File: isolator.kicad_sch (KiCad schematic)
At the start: 120 parts, among them J1 HOST, J2 USB_C_Receptacle_PowerOnly_6P, J3 USB_A, J4 USB_A, J5 USB_C_Receptacle_USB2.0_16P, J6 USB_C_Receptacle_USB2.0_16P, Q1 2N7002, Q2 2N7002, T1 750313638, U1 ADuM4165, U10 TPS2553DBV, U11 TPS2553DBV, U12 TPS2553DBV, U13 TLV7041DBV, U14 TLV7041DBV, U15 NUP4202, U16 NUP4202, U17 NUP4202, U18 NUP4202, U2 NUP4202, U3 NUP4202, U4 USB2514B_Bi, U5 SN6505BDBV, U6 MIC29302WU, U7 TPS2121, U8 AP2112K-3.3, U9 TPS2553DBV, Y1 24M 8pF, Y2 24M 12pF

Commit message: chore(sch): carry GUI session edits; restore U7 OV2 ground wires lost in GUI edit
Co-Authored-By: Claude Fable 5 <noreply@anthropic.com>
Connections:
- net HOST_D+: now also U2.1; no longer U2.6
- net HOST_D-: now also U2.6; no longer U2.1

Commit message: feat: swap NUP4202 ESD for flow-through USBLC6-2SC6 (sch+pcb), symmetric USB pair routing
Replaces all six NUP4202 SOT-363 ESD arrays (U2 host, U3 hub-upstream,
U15-U18 downstream ports) with USBLC6-2SC6 in SOT-23-6.

The NUP4202 pinout forced each USB HS pair to split - one line off the top
of the package, the other off the bottom - so the pairs could not be routed
symmetrically. The USBLC6-2SC6 is flow-through: I/O1 appears on pins 1 and 6,
I/O2 on pins 3 and 4, so a pair enters one edge and leaves the opposite edge
at constant 1.9 mm spacing with no crossing.

Schematic:
- lib_symbols cache: NUP4202 removed, USBLC6-2SC6 added (flattened from the
  stock Power_Protection library, which defines it as extends USBLC6-2P6).
- All six sites redrawn flow-through at rot 0: D+ on pins 1/6 (left/right),
  D- on pins 3/4, VBUS up, GND down. Stale pin-3/4 no_connects removed.
- Properties: Value/Footprint/Datasheet updated; MPN USBLC6-2SC6,
  Manufacturer STMicroelectronics, LCSC C2687116 (SOT-23-6 variant - the
  commonly quoted C7519 is the SOT-23-6L package and does not match).
- Symbol UUIDs preserved so the schematic<->PCB links survive.

PCB:
- SOT-363 footprints replaced with SOT-23-6, entry row (pads 1/2/3) facing
  the connector/source side at each site.
- U17 and U18 nudged (the SOT-23-6 is 1.6 mm wider than the SOT-363 and
  collided with J5/J6): U17 160.5,95.0 -> 159.3,95.0; U18 160.5,110.0 ->
  159.4,106.7 with its refdes moved above the body to clear C43.

Gates: schematic ERC exit 0 (0 errors, no new warnings); PCB reloads;
DRC no new violation types, creepage still exactly 1 (the known C49 finding),
silk_overlap 11->10; unconnected 333->345 (+12, expected: pads 3/4 now carry
real nets instead of unconnected-(Ux-PadN)); 36/36 pads verified identical
between the schematic netlist export and the board.

Spec updated, including the eval-board rationale sentence: the core still
matches EVAL-ADuM4165 except for this deliberate ESD deviation.

Co-Authored-By: Claude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
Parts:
- U15, U16, U17, U18, U2, U3: value NUP4202 -> USBLC6-2SC6; footprint Package_TO_SOT_SMD:SOT-363_SC-70-6 -> Package_TO_SOT_SMD:SOT-23-6; symbol Power_Protection:NUP4202 -> Power_Protection:USBLC6-2SC6; LCSC C2937014 -> C2687116; MPN NUP4202W1T2G -> USBLC6-2SC6; Manufacturer onsemi -> STMicroelectronics
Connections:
- net HOST_D+: now also U2.6 (I/O1)
- net HOST_D-: now also U2.3 (I/O2), U2.4 (I/O2); no longer U2.6
- net ISO_D+: now also U3.1 (I/O1)
- net ISO_D-: now also U3.3 (I/O2), U3.4 (I/O2); no longer U3.1
- net P1_D+: now also U15.1 (I/O1)
- net P1_D-: now also U15.3 (I/O2), U15.4 (I/O2); no longer U15.1
- net P2_D+: now also U16.1 (I/O1)
- net P2_D-: now also U16.3 (I/O2), U16.4 (I/O2); no longer U16.1
- net P3_D+: now also U17.1 (I/O1)
- net P3_D-: now also U17.3 (I/O2), U17.4 (I/O2); no longer U17.1
- net P4_D+: now also U18.1 (I/O1)
- net P4_D-: now also U18.3 (I/O2), U18.4 (I/O2); no longer U18.1
- no-connect marks 19 -> 7

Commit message: feat(pcb): extend barrier slot under C49 (now 2220), rounded corners with concentric mounting holes, corrected 90R diff geometry per JLC-7628
Co-Authored-By: Claude Fable 5 <noreply@anthropic.com>
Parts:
- C49: footprint Capacitor_SMD:C_1812_4532Metric -> Capacitor_SMD:C_2220_5750Metric
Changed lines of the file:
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@@
 			)
 		)
-		(property "Footprint" "Capacitor_SMD:C_1812_4532Metric"
+		(property "Footprint" "Capacitor_SMD:C_2220_5750Metric"
 			(at 185.42 40.64 0)
 			(hide yes)

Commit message: wip(pcb): routing session 2 — GND stitching pours, more escapes
Co-Authored-By: Claude Fable 5 <noreply@anthropic.com>
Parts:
- added C50: 100n, Capacitor_SMD:C_0603_1608Metric, symbol Device:C_Small
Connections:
- net GND1: now also C50.2
- net GND2: no longer U7.4 (OV2)
- net VBUS_HOST: now also C50.1
- net at T1.1 (N1): now also U5.3 (D2); no longer U5.1 (D1)
- net at T1.3 (N2): now also U5.1 (D1); no longer U5.3 (D2)

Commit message: fix: decoupling audit fixes — tantalum C10 (T491D, polarity-correct), R36 330R min-load, 22u port bulk, re-seat ISO_5V bypass caps at their ICs per datasheet distances
Co-Authored-By: Claude Fable 5 <noreply@anthropic.com>
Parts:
- C10: footprint Capacitor_SMD:C_1210_3225Metric -> Capacitor_Tantalum_SMD:CP_EIA-7343-31_Kemet-D; MPN TMK325ABJ476MM-P -> T491D476K010AT
- C38, C41, C44, C47: value 10u -> 22u; MPN CL21A106KAYNNNE -> GRM21BR61A226ME44L
- R36: value 1k -> 330R; MPN RC0603FR-071KL -> RC0603FR-07330RL
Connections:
- net DCDC_5V: now also C10.1; no longer C10.2
- net GND2: now also C10.2, U7.4 (OV2); no longer C10.1
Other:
- moved on the sheet: C10
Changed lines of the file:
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@@
 			)
 		)
-		(property "Value" "10u"
+		(property "Value" "22u"
 			(at 171.45 345.4462 0)
 			(show_name no)
@@
 			)
 		)
-		(property "MPN" "CL21A106KAYNNNE"
+		(property "MPN" "GRM21BR61A226ME44L"
 			(at 168.91 344.17 0)
 			(hide yes)
@@
 			)
 		)
-		(property "Value" "10u"
+		(property "Value" "22u"
 			(at 133.35 400.0562 0)
 			(show_name no)
@@
 			)
 		)
-		(property "MPN" "CL21A106KAYNNNE"
+		(property "MPN" "GRM21BR61A226ME44L"
 			(at 130.81 398.78 0)
 			(hide yes)
@@
 			)
 		)
-		(property "Value" "10u"
+		(property "Value" "22u"
 			(at 294.64 345.4462 0)
 			(show_name no)
@@
 			)
 		)
-		(property "MPN" "CL21A106KAYNNNE"
+		(property "MPN" "GRM21BR61A226ME44L"
 			(at 292.1 344.17 0)
 			(hide yes)
@@
 			)
 		)
-		(property "Value" "10u"
+		(property "Value" "22u"
 			(at 83.82 345.4462 0)
 			(show_name no)
@@
 			)
 		)
-		(property "MPN" "CL21A106KAYNNNE"
+		(property "MPN" "GRM21BR61A226ME44L"
 			(at 81.28 344.17 0)
 			(hide yes)
@@
 	(symbol
 		(lib_id "Device:C_Small")
-		(at 619.76 44.45 180)
+		(at 619.76 44.45 0)
 		(unit 1)
 		(body_style 1)
@@
 			)
 		)
-		(property "Footprint" "Capacitor_SMD:C_1210_3225Metric"
+		(property "Footprint" "Capacitor_Tantalum_SMD:CP_EIA-7343-31_Kemet-D"
 			(at 619.76 44.45 0)
 			(hide yes)
@@
 			)
 		)
-		(property "MPN" "TMK325ABJ476MM-P"
+		(property "MPN" "T491D476K010AT"
 			(at 619.76 44.45 0)
 			(hide yes)
@@
 			)
 		)
-		(property "Value" "1k"
+		(property "Value" "330R"
 			(at 504.19 303.5299 0)
 			(show_name no)
@@
 			)
 		)
-		(property "MPN" "RC0603FR-071KL"
+		(property "MPN" "RC0603FR-07330RL"
 			(at 501.65 302.26 0)
 			(hide yes)
@@
 		)
 	)
+	(wire
+		(pts
+			(xy 193.04 176.53) (xy 199.39 176.53)
+		)
+		(stroke
+			(width 0)
+			(type default)
+		)
+	)
+	(wire
+		(pts
+			(xy 195.58 181.61) (xy 195.58 176.53)
+		)
+		(stroke
+			(width 0)
+			(type default)
+		)
+	)
+	(wire
+		(pts
+			(xy 195.58 176.53) (xy 201.93 176.53)
+		)
+		(stroke
+			(width 0)
+			(type default)
+		)
+	)

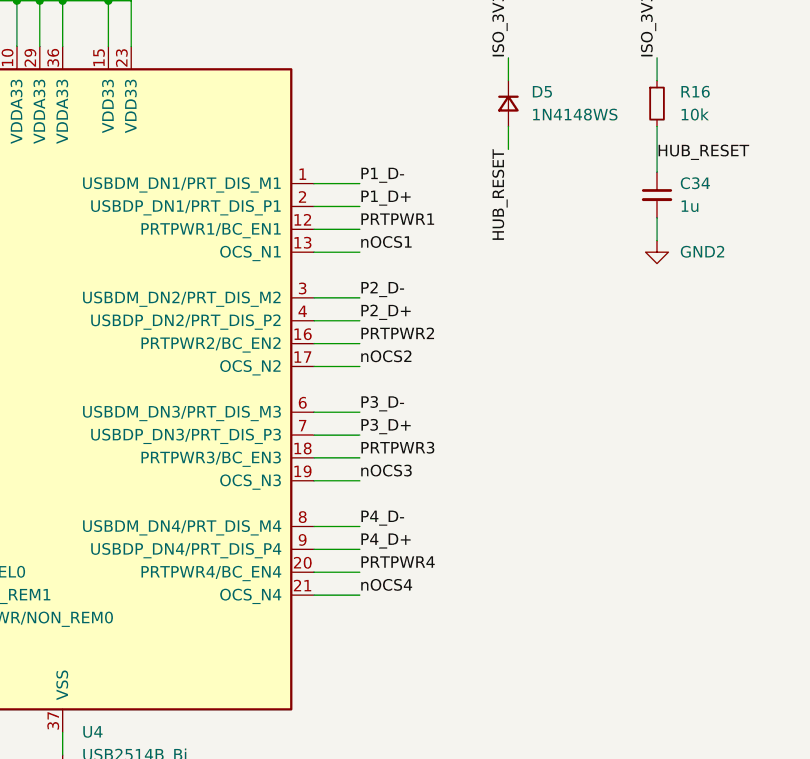
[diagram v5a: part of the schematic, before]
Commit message: feat: swap hub port bundles 1<->4 2<->3 for crossing-free fanout (sch+pcb)
U4 (USB2514B) is at rot 0 with all four downstream port pin bundles on its
WEST edge, while all four ports are on the far EAST side and are approached
heading east.  Any path from "heading west" to "heading east" is a 180 degree
turn, which reverses the transverse order of the ribbon: the pairs left U4 as
P1,P2,P3,P4 (north->south) and arrived as P4,P3,P2,P1, while the destinations
need P1,P2,P3,P4.  That is a full reversal of four items = 6 pair-to-pair
crossings, i.e. at least three crossunders (12 vias) on 480 Mbit/s pairs.
No rotation of U4 fixes it - handedness is preserved under rotation.

Hub ports 1-4 are functionally identical, so the fix is a net swap, not copper.
Full bundles move together (data pair + PRTPWR/BC_EN + OCS_N) so each port's
power switch and fault line stay with their own data pair:

  hub port1 <- port4   hub port2 <- port3
  hub port3 <- port2   hub port4 <- port1

Schematic: the 16 net labels on U4's downstream pin column (x = 463.55) were
renamed.  Nothing else moved - connector-side nets, TPS2553 switches, ILIM
resistors, ESD parts and VBUS are untouched.

PCB: the 16 affected U4 pads were re-netted in a mutation-only session, each
one cross-checked against a fresh `kicad-cli sch export netlist` before saving;
all 37 U4 pads verified to match the netlist afterwards.

Verification
  ERC severity-error: 0 violations, exit 0
  /PnD+- now = {U4 <new pin>, USBLC6 x2, connector}
    P1 -> U4 pins 8/9 (was 1/2)   P2 -> pins 6/7   P3 -> pins 3/4   P4 -> 1/2
  /PRTPWRn = exactly {U4 pin, TPS2553 pin 3} for all four
  /nOCSn   = {U4 pin, TPS2553 pin 4, pull-up} for all four
  GND1 n GND2 = {U1, C49} unchanged
  DRC unchanged: 102 violations, 170 unconnected, shorting 0, dangling 0

Co-Authored-By: Claude Fable 5 <noreply@anthropic.com>
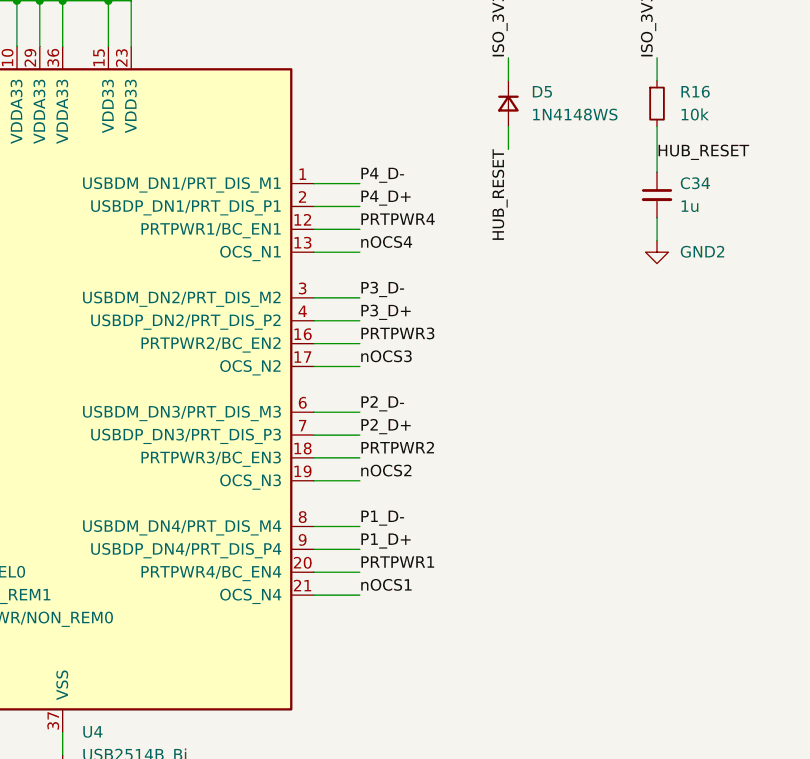
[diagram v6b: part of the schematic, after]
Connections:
- net P1_D+: now also U4.9 (USBDP_DN4/PRT_DIS_P4); no longer U4.2 (USBDP_DN1/PRT_DIS_P1)
- net P1_D-: now also U4.8 (USBDM_DN4/PRT_DIS_M4); no longer U4.1 (USBDM_DN1/PRT_DIS_M1)
- net P2_D+: now also U4.7 (USBDP_DN3/PRT_DIS_P3); no longer U4.4 (USBDP_DN2/PRT_DIS_P2)
- net P2_D-: now also U4.6 (USBDM_DN3/PRT_DIS_M3); no longer U4.3 (USBDM_DN2/PRT_DIS_M2)
- net P3_D+: now also U4.4 (USBDP_DN2/PRT_DIS_P2); no longer U4.7 (USBDP_DN3/PRT_DIS_P3)
- net P3_D-: now also U4.3 (USBDM_DN2/PRT_DIS_M2); no longer U4.6 (USBDM_DN3/PRT_DIS_M3)
- net P4_D+: now also U4.2 (USBDP_DN1/PRT_DIS_P1); no longer U4.9 (USBDP_DN4/PRT_DIS_P4)
- net P4_D-: now also U4.1 (USBDM_DN1/PRT_DIS_M1); no longer U4.8 (USBDM_DN4/PRT_DIS_M4)
- net PRTPWR1: now also U4.20 (PRTPWR4/BC_EN4); no longer U4.12 (PRTPWR1/BC_EN1)
- net PRTPWR2: now also U4.18 (PRTPWR3/BC_EN3); no longer U4.16 (PRTPWR2/BC_EN2)
- net PRTPWR3: now also U4.16 (PRTPWR2/BC_EN2); no longer U4.18 (PRTPWR3/BC_EN3)
- net PRTPWR4: now also U4.12 (PRTPWR1/BC_EN1); no longer U4.20 (PRTPWR4/BC_EN4)
- net nOCS1: now also U4.21 (OCS_N4); no longer U4.13 (OCS_N1)
- net nOCS2: now also U4.19 (OCS_N3); no longer U4.17 (OCS_N2)
- net nOCS3: now also U4.17 (OCS_N2); no longer U4.19 (OCS_N3)
- net nOCS4: now also U4.13 (OCS_N1); no longer U4.21 (OCS_N4)
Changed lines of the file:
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@@
 		)
 	)
-	(label "P1_D+"
+	(label "P4_D+"
 		(at 463.55 153.67 0)
 		(effects
@@
 		)
 	)
-	(label "P3_D+"
+	(label "P2_D+"
 		(at 463.55 179.07 0)
 		(effects
@@
 		)
 	)
-	(label "P4_D+"
+	(label "P1_D+"
 		(at 463.55 191.77 0)
 		(effects
@@
 		)
 	)
-	(label "nOCS2"
+	(label "nOCS3"
 		(at 463.55 171.45 0)
 		(effects
@@
 		)
 	)
-	(label "PRTPWR4"
+	(label "PRTPWR1"
 		(at 463.55 194.31 0)
 		(effects
@@
 		)
 	)
-	(label "P2_D+"
+	(label "P3_D+"
 		(at 463.55 166.37 0)
 		(effects
@@
 		)
 	)
-	(label "P2_D-"
+	(label "P3_D-"
 		(at 463.55 163.83 0)
 		(effects
@@
 		)
 	)
-	(label "PRTPWR3"
+	(label "PRTPWR2"
 		(at 463.55 181.61 0)
 		(effects
@@
 		)
 	)
-	(label "nOCS4"
+	(label "nOCS1"
 		(at 463.55 196.85 0)
 		(effects
@@
 		)
 	)
-	(label "PRTPWR2"
+	(label "PRTPWR3"
 		(at 463.55 168.91 0)
 		(effects
@@
 		)
 	)
-	(label "nOCS1"
+	(label "nOCS4"
 		(at 463.55 158.75 0)
 		(effects
@@
 		)
 	)
-	(label "P4_D-"
+	(label "P1_D-"
 		(at 463.55 189.23 0)
 		(effects
@@
 		)
 	)
-	(label "PRTPWR1"
+	(label "PRTPWR4"
 		(at 463.55 156.21 0)
 		(effects
@@
 		)
 	)
-	(label "P1_D-"
+	(label "P4_D-"
 		(at 463.55 151.13 0)
 		(effects
@@
 		)
 	)
-	(label "P3_D-"
+	(label "P2_D-"
 		(at 463.55 176.53 0)
 		(effects
@@
 		)
 	)
-	(label "nOCS3"
+	(label "nOCS2"
 		(at 463.55 184.15 0)
 		(effects

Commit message: wip(4port): save in-progress 4-port schematic/PCB edits before archiving
Snapshot of the uncommitted work on the 4-port isolator so it is preserved
before the repo collapses to the single-port design at the root.

State of this snapshot: ERC reports 3 errors, all U7 (TPS2121) pin 4 OV2
disconnected. That is pre-existing, in-progress work on the 4-port design --
it is NOT a regression introduced here and is deliberately left unfixed.

This commit is the tip of branch 4port-archive; main proceeds without the
4-port project.

Co-Authored-By: Claude Opus 5 <noreply@anthropic.com>
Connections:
- net GND2: no longer U7.4 (OV2)

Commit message: refactor: collapse repo to the single-port isolator at the root
The single-port design is the one that ships, so it moves up from v1/ and
becomes the only KiCad project in the repo. The 4-port design is archived on
branch 4port-archive (tip ef23a53) and removed from main.

Moved (via git mv, history preserved):
  v1/isolator-v1.kicad_{sch,pcb,pro,dru} -> isolator.kicad_{sch,pcb,pro,dru}
  v1/isolator-v1-bom.csv                 -> isolator-bom.csv
  v1/{sym,fp}-lib-table                  -> {sym,fp}-lib-table
  analysis-v1/                           -> analysis/

Deleted (4-port project and its artifacts): isolator.kicad_{sch,pcb,pro,prl,dru},
isolator-erc.rpt, isolator-backups/, analysis/, logs/. Kept isolator-lib.kicad_sym,
isolator-lib.pretty/, datasheets/, docs/, tools/.

Path and self-reference fixes the move required:
  - {sym,fp}-lib-table URIs: ${KIPRJMOD}/../isolator-lib.* -> ${KIPRJMOD}/isolator-lib.*
  - isolator.kicad_pro: meta.filename and schematic.top_level_sheets[0].filename/name,
    plus sheets[0]. The sheet UUID already matched the schematic root uuid
    (00000000-0000-0000-0000-000000000001) and was left alone. kicad-cli never
    reads these fields, so nothing but a GUI open would have caught them.
  - isolator.kicad_sch: 62 (project "isolator-v1") instance blocks -> "isolator",
    so the GUI keeps its per-project symbol instance data.
  - Schematic text block "V1 LAYOUT CONSTRAINTS -- BINDING" -> "LAYOUT CONSTRAINTS
    -- BINDING"; title block "Isolated USB 2.0 Cable — v1" -> "Isolated USB 2.0
    Cable". Rev "v1.0" left as-is: that is a revision, not a design name.
  - docs/superpowers/{specs,plans,reviews}/*.md: paths updated, "v1" as a design
    name rewritten to "the isolator", "v2" to "the archived 4-port design".
    References to the 4-port files now read 4port-archive:isolator.kicad_sch, since
    that path at the root means the single-port design now. Every doc carries a
    dated banner explaining the restructure; past-tense decisi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
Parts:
- removed C16, C17, C19, C20, C23, C24, C25, C26, C27, C28, C29, C30, C31, C35, C36, C37, C39, C40, C42, C43, C45, C46, C48: 0.1u, Capacitor_SMD:C_0603_1608Metric, symbol Device:C_Small
- removed C18: 47u, Capacitor_SMD:C_1210_3225Metric, symbol Device:C_Small
- removed C21, C22, C34: 1u, Capacitor_SMD:C_0603_1608Metric, symbol Device:C_Small
- removed C32, C33: 18p, Capacitor_SMD:C_0603_1608Metric, symbol Device:C_Small
- removed C38, C41, C44, C47: 22u, Capacitor_SMD:C_0805_2012Metric, symbol Device:C_Small
- removed C49: 1nF 2kV DNP, Capacitor_SMD:C_2220_5750Metric, symbol Device:C_Small
- removed C50: 100n, Capacitor_SMD:C_0603_1608Metric, symbol Device:C_Small
- removed D5: 1N4148WS, Diode_SMD:D_SOD-323, symbol Device:D_Small
- removed D6: LED, LED_SMD:LED_0603_1608Metric, symbol Device:LED
- removed J2: USB_C_Receptacle_PowerOnly_6P, Connector_USB:USB_C_Receptacle_GCT_USB4125-xx-x_6P_TopMnt_Horizontal, symbol Connector:USB_C_Receptacle_PowerOnly_6P
- removed J3, J4: USB_A, Connector_USB:USB_A_Molex_67643_Horizontal, symbol Connector:USB_A
- removed J5, J6: USB_C_Receptacle_USB2.0_16P, Connector_USB:USB_C_Receptacle_HRO_TYPE-C-31-M-12, symbol Connector:USB_C_Receptacle_USB2.0_16P
- removed Q1, Q2: 2N7002, Package_TO_SOT_SMD:SOT-23, symbol Transistor_FET:2N7002
- removed R11, R23, R24: 47k, Resistor_SMD:R_0603_1608Metric, symbol Device:R_Small
- removed R12: 35.7k, Resistor_SMD:R_0603_1608Metric, symbol Device:R_Small
- removed R13, R16, R21, R22: 10k, Resistor_SMD:R_0603_1608Metric, symbol Device:R_Small
- removed R14, R35: 1k, Resistor_SMD:R_0603_1608Metric, symbol Device:R_Small
- removed R15: 12.0k, Resistor_SMD:R_0603_1608Metric, symbol Device:R_Small
- removed R17, R18, R19, R20, R25, R26: 100k, Resistor_SMD:R_0603_1608Metric, symbol Device:R_Small
- removed R27, R28, R29, R30: 40.2k, Resistor_SMD:R_0603_1608Metric, symbol Device:R_Small
- removed R31, R32, R33, R34: 56k, Resistor_SMD:R_0603_1608Metric, symbol Device:R_Small
- removed R36: 330R, Resistor_SMD:R_0603_1608Metric, symbol Device:R_Small
- removed U10, U11, U12, U9: TPS2553DBV, Package_TO_SOT_SMD:SOT-23-6, symbol isolator-lib:TPS2553DBV
- removed U13, U14: TLV7041DBV, Package_TO_SOT_SMD:SOT-23-5, symbol Comparator:TLV7041DBV
- removed U15, U16, U17, U18: USBLC6-2SC6, Package_TO_SOT_SMD:SOT-23-6, symbol Power_Protection:USBLC6-2SC6
- removed U4: USB2514B_Bi, Package_DFN_QFN:QFN-36-1EP_6x6mm_P0.5mm_EP3.7x3.7mm, symbol Interface_USB:USB2514B_Bi
- removed U5: SN6505BDBV, Package_TO_SOT_SMD:SOT-23-6, symbol Power_Management:SN6505BDBV
- removed U6: MIC29302WU, Package_TO_SOT_SMD:TO-263-5_TabPin3, symbol Regulator_Linear:MIC29302WU
- removed U7: TPS2121, Package_DFN_QFN:Texas_VQFN-HR-12_2x2.5mm_P0.5mm, symbol isolator-lib:TPS2121
- removed U8: AP2112K-3.3, Package_TO_SOT_SMD:SOT-23-5, symbol Regulator_Linear:AP2112K-3.3
- removed Y2: 24M 12pF, Crystal:Crystal_SMD_3225-4Pin_3.2x2.5mm, symbol Device:Crystal_GND24_Small
- added CY1: 1nF Y1 400VAC, isolator-lib:C_Disc_D7.0mm_W5.5mm_P14.00mm, symbol Device:C
- added D5, D6: T6V0S5A-7, Diode_SMD:D_SOD-523, symbol Device:D_TVS
- added J2: PORT, Connector_USB:USB_C_Receptacle_HRO_TYPE-C-31-M-12, symbol Connector:USB_C_Receptacle_USB2.0_16P
- added Q1: 2N7002, Package_TO_SOT_SMD:SOT-23, symbol isolator-lib:2N7002
- added U4: SN6505BDBV, Package_TO_SOT_SMD:SOT-23-6, symbol Power_Management:SN6505BDBV
- added U5: TLV76750DGNR, Package_SO:HVSSOP-8-1EP_3x3mm_P0.65mm_EP1.57x1.89mm, symbol isolator-lib:TLV76750DGNR
- added U6: TPS2553DBV, Package_TO_SOT_SMD:SOT-23-6, symbol isolator-lib:TPS2553DBV
- C10: value 47u -> 47uF; footprint Capacitor_Tantalum_SMD:CP_EIA-7343-31_Kemet-D -> Capacitor_SMD:C_1210_3225Metric; MPN T491D476K010AT -> TMK325ABJ476MM-P; Tolerance ±20% -> (none)
- C11, C13, C15, C6, C9: value 0.1u -> 100n
- C12: value 10u -> 100n; footprint Capacitor_SMD:C_0805_2012Metric -> Capacitor_SMD:C_0603_1608Metric; LCSC C15850 -> C14663; MPN CL21A106KAYNNNE -> CC0603KRX7R9BB104; Manufacturer Samsung Electro-Mechanics -> YAGEO
- C14: value 10u -> 22u; MPN CL21A106KAYNNNE -> GRM21BR61A226ME44L
- C3, C7: value 10u -> 4.7uF; LCSC C15850 -> C162427; MPN CL21A106KAYNNNE -> GRM21BR71E475KA73L; Manufacturer Samsung Electro-Mechanics -> Murata; Tolerance ±10% -> (none)
- C8: value 47u -> 47uF; Tolerance ±20% -> (none)
- R3: value 30.1k -> 93.1k; LCSC C137745 -> C273780; MPN RC0603FR-0730K1L -> RC0603FR-0793K1L
- R4: value 10k -> 100k; LCSC C98220 -> C14675; MPN RC0603FR-0710KL -> RC0603FR-07100KL
- R5: value 5.1k -> 330; LCSC C105580 -> C105881; MPN RC0603FR-075K1L -> RC0603FR-07330RL
- R6: value 5.1k -> 3.01k; LCSC C105580 -> C137732; MPN RC0603FR-075K1L -> RC0603FR-073K01L
- R7: value 16.9k -> 56k; LCSC C137789 -> C114630; MPN RC0603FR-0716K9L -> RC0603FR-0756KL
- R8: value 10k -> 56k; LCSC C98220 -> C114630; MPN RC0603FR-0710KL -> RC0603FR-0756KL
- R9: now not fitted; now left out of the parts list
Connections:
- net EXT_CC1 is gone; now on net ISO_5V: R5.1
- net EXT_CC2 is gone; now on net ISO_5V: R6.1
- net PR1_SENSE is gone; now on net GND2: R10.2
- net n3A_DET is gone; now on net PGOOD2: R9.2
- net DCDC_RAW: now also C8.1, C9.1, U5.5 (EN), U5.8 (IN); no longer C8.2, C9.2
- net GND1: now also C6.2, C7.2, CY1.2, D5.2 (A2), U4.4 (GND), U4.6 (CLK); no longer C6.1, C7.1
- net GND2: now also C11.2, C8.2, C9.2, R3.2, CY1.1, D6.2 (A2), J2.A1 (GND), J2.A12 (GND), J2.B1 (GND), J2.B12 (GND), J2.SH (SHIELD), Q1.2 (S), U5.4 (GND), U5.6 (GND), U5.9 (PAD), U6.2 (GND); no longer C11.1, C8.1, C9.1, D4.1 (K), R4.1, R5.2, R6.2, R8.2
- net ILIM_SET: now also R3.1, U6.5 (ILIM)
- net ISO_5V: now also C10.1, C11.1, C12.1, R4.1, U5.1 (OUT), U5.2 (SNS), U6.1 (IN), U6.3 (EN); no longer U3.5 (VBUS)
- net PGOOD2: now also R10.1, Q1.1 (G)
- net VBUS_HOST: now also C6.1, C7.1, D5.1 (A1), U4.2 (VCC), U4.5 (EN); no longer C6.2, C7.2
- net VDD2: now also C13.1, R9.1
- net nFAULT: now reaches R4.2
- net nFAULT: now also D4.1 (K), U6.4 (~{FAULT}); no longer R3.2
- net RECT_B: now reaches D2.2 (A), T1.4 (N4)
- net RECT_A: now reaches D1.2 (A), T1.6 (N3)
- net PP_B: now reaches T1.1 (N1)
- net PP_B: now also U4.3 (D2)
- net PP_A: now reaches T1.3 (N2)
- net PP_A: now also U4.1 (D1)
- removed net DCDC_5V: C10.1, C11.2, R3.1
- removed net EXT_5V: C12.1, C13.1, C14.1, C15.1, R10.1
- net ISO_3V3 renamed PORT_VBUS
- net PORT_VBUS: now also C14.1, C15.1, R8.1, U3.5 (VBUS), D6.1 (A1), J2.A4 (VBUS), J2.A9 (VBUS), J2.B4 (VBUS), J2.B9 (VBUS), U6.6 (OUT); no longer R9.1
- net ISO_D+ renamed PORT_D+
- net PORT_D+: now also J2.A6 (D+), J2.B6 (D+)
- net ISO_D- renamed PORT_D-
- net PORT_D-: now also J2.A7 (D-), J2.B7 (D-)
- net PGOOD_LED_A renamed PG_LED_A
- net PG_LED_A: now also R6.2
- net PGOOD_LED_K renamed PG_LED_K
- net PG_LED_K: now also Q1.3 (D)
- net ST_LED renamed FAULT_LED_A
- net FAULT_LED_A: now also R5.2
- net VTH renamed PORT_CC1
- net PORT_CC1: now also J2.A5 (CC1); no longer R8.1
- new net PORT_CC2: J2.B5 (CC2), R8.2
- no-connect marks 7 -> 4
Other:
- note added: "1. Board 50 mm wide (Hammond 1455C slot), 120 mm length (1455C1202), 4 layers, 90 Ω differential pairs. 2. ALL COPPER PULLED BACK ≥1 mm (target 2 mm) FROM BOTH LONG EDGES, every layer, full length. The extrusion's aluminium slots grip those edges; edge copper lets the enclosure short GND1 to GND2. 3. ESD arrays (U2, U3) within 5 mm of the connector pins they protect. Array GND pin on its own via 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"
- note added: "CY1 -- BARRIER STITCHING (POPULATED, NOT DNP)"
- note added: "CY1 -- barrier stitching. POPULATED, not DNP. Gives GND2's ESD current a defined return to GND1 instead of forcing it through the ADuM4165 die. Y1 safety-rated, 14 mm pitch, clears the 8.3 mm barrier. Do NOT substitute v2's 2220 SMD part -- its body spans only 5.7 mm and would cut the barrier below 8.3 mm."
- note added: "DOWNSTREAM ESD + USB-C PORT (GND2)"
- note added: "FULL-WAVE RECTIFIER + TLV76750 5V LDO (GND2)"
- note added: "ISOLATOR U1 (ADuM4165) -- SIDE 1 (GND1) / SIDE 2 (GND2)"
- note added: "LAYOUT CONSTRAINTS -- BINDING"
- note added: "PGOOD is PUSH-PULL (ADuM4165 Table 18, p.15) -- drives both High and Low, never open-drain. R10 stays populated, R9 stays DNP -- never populate both. If R9 is ever populated, pull-up MUST go to VDD2, NEVER ISO_5V. PGOOD abs max = VDD2+0.5V."
- note added: "SN6505B PUSH-PULL DRIVER + T1 TRANSFORMER (GND1 PRIMARY)"
- note added: "TPS2553 PORT SWITCH (GND2)"
- note added: "USB-C HOST PORT (GND1)"
- note removed: "DNP -- EMI stitching provision, see spec"
- note removed: "DOWNSTREAM PORTS"
- note removed: "EXTERNAL POWER + PRIORITY MUX"
- note removed: "INDICATORS"
- note removed: "ISOLATED DC-DC"
- note removed: "ISOLATION BARRIER"
- note removed: "UPSTREAM HOST (GND1)"
- note removed: "USB HUB"
- title: (none) -> Isolated USB 2.0 Cable
